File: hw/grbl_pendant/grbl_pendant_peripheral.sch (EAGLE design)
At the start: 29 parts, among them CON1 MOLEX-53261-0671, IC2 FT232RL, Q1 14.7456 MHz, X1 PN61729-S

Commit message: sch/brd files updated
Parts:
- removed C1, C8, C9: 10u, rcl:C-EUC0805
- removed C10: 100n, rcl:C-EUC0805
- removed C2, C4: 20p, rcl:C-EUC0603K
- removed C3: 100n, rcl:C-EUC0603
- removed C5, C6, C7: 100n, rcl:C-EUC0603K
- removed CON1: MOLEX-53261-0671, SchlegelAr_Master:MOLEX-53261-0671
- removed FERRIT1, FERRIT2, FERRIT3: (no value), rcl:R-EU_M0805
- removed IC2: FT232RL, ftdichip:FT232RL
- removed JP1: (no value), pinhead-2:PINHD-2X08_2.54
- removed Q1: 14.7456 MHz, crystal:CRYSTALHC49UP
- removed R2, R3, R7: 220R, rcl:R-EU_R0603
- removed R4, R5, R6: 100R, rcl:R-EU_R0603
- removed U$2: ARDUINONANO, rocketfarm:ARDUINONANO
- removed X1: PN61729-S, con-berg:PN61729-S
- removed X2, X3: (no value), con-subd:F25HPS
- added C11: 100n, rcl:C-EUC0603K
- added ENC1: ENCODER, encoder:ENCODER
- added IC1: 74HC595D, 74xx-eu:74HC595D
- added LED1, LED2, LED3, LED4, LED5, LED6, LED7, LED8: (no value), led:LED5MM
- added R10, R11, R12, R13, R14, R15, R8, R9: 680R, rcl:R-EU_R0603
- added R16, R17, R18, R19, R20, R21, R22, R23, R24, R25: 10k, rcl:R-EU_R0603
- added S1, S2, S3, S4, S5, S6, S7: (no value), switch-omron:10-XX
- added X4: (no value), con-subd:F25HPS
- R1: value 220R -> 10k; device rcl:R-EU_R0603 -> SchlegelAr_Master:35WR5KLFTR
- U$1: value MEGA162MA*A* -> LCD-HD447804-HOLES20X4-4HOLES; device avr-7:MEGA162MA*A* -> HD44780LCD:LCD-HD447804-HOLES20X4-4HOLES
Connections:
- removed net !RESET: CON1.RESET
- removed net COOLING_ENABLE: U$2.A3, X2-17.F
- removed net CYCLE_START/RESUME: U$2.A2, X2-18.F
- removed net FEED/HOLD: U$2.A1, X2-19.F
- removed net LED_SHIFT_SCK: U$1.(WR)PD6
- removed net LIMIT_INT_X: C9.2, FERRIT3.2, R1.2, R4.1
- removed net LIMIT_INT_Y: C8.2, FERRIT2.2, R3.2, R5.1
- removed net LIMIT_INT_Z: C1.2, FERRIT1.2, R2.2, R6.1
- removed net LIMIT_X: FERRIT3.1, X2-25.F
- removed net LIMIT_X_DEBOUNCED: R4.2, U$2.D9
- removed net LIMIT_Y: FERRIT2.1, X2-24.F
- removed net LIMIT_Y_DEBOUNCED: R5.2, U$2.D10
- removed net LIMIT_Z: FERRIT1.1, X2-23.F
- removed net LIMIT_Z_DEBOUNCED: R6.2, U$2.D11
- removed net MISO: CON1.MISO, JP1.13, JP1.14, U$1.(MISO)PB6
- removed net MOSI: CON1.MOSI, JP1.10, JP1.9, U$1.(MOSI)PB5
- removed net N$7: C4.2, Q1.2, U$1.XTAL2
- removed net N$8: C2.1, Q1.1, U$1.XTAL1
- removed net RESET/ABORT: U$2.A0, X2-20.F
- removed net RESET_AVR: U$1.RESET, U$2.RESET1, X2-21.F
- removed net RXD_BRIDGE: U$1.(RXD1)PB2, U$2.D1/TX
- removed net RXD_PC: IC2.RXD, U$1.(TXD0)PD1
- removed net SCK: CON1.SCK, JP1.11, JP1.12, U$1.(SCK)PB7
- removed net SD_IO_1: U$1.(AD7)PA7
- removed net SD_IO_2: U$1.(T1)PB1
- removed net SD_IO_3: U$1.(T0)PB0
- removed net SD_IO_4: U$1.(RD)PD7
- removed net SPINDLE_DIR: U$2.D13, X2-16.F
- removed net SPINDLE_ENABLE: U$2.D12, X2-1.F
- removed net SS: JP1.7, JP1.8, U$1.(SS)PB4
- removed net STEPPER_DISABLE: U$2.D8, X2-15.F
- removed net TXD_BRIDGE: U$1.(TXD1)PB3, U$2.D0/RX
- removed net TXD_PC: IC2.TXD, U$1.(RXD0)PD0
- removed net USBDM: IC2.USBDM, X1.2
- removed net USBDP: IC2.USBDP, X1.3
- removed net X_DIR: U$2.D5, X2-2.F
- removed net X_STEP: U$2.D2, X2-3.F
- removed net Y_DIR: U$2.D6, X2-4.F
- removed net Y_STEP: U$2.D3, X2-5.F
- removed net Z_DIR: U$2.D7, X2-6.F
- removed net Z_PROBE: R7.2, U$2.A5, X2-22.F
- removed net Z_STEP: U$2.D4, X2-7.F
- new net N$1: IC1A.QD, R11.1
- new net N$10: IC1A.QG, R14.1
- new net N$11: IC1A.QH, R15.1
- new net N$12: LED1.A, R8.2
- new net N$13: LED2.A, R9.2
- new net N$14: LED3.A, R10.2
- new net N$15: LED4.A, R11.2
- new net N$16: LED5.A, R12.2
- new net N$17: LED6.A, R13.2
- new net N$18: LED7.A, R14.2
- new net N$19: LED8.A, R15.2
- new net N$2: IC1A.QA, R8.1
- new net N$3: IC1A.QB, R9.1
- new net N$4: IC1A.QC, R10.1
- new net N$6: IC1A.QE, R12.1
- new net N$9: IC1A.QF, R13.1
- net +5V: now also C11.1, IC1A.SCL, IC1P.VCC, R1.E, R16.1, R17.1, R18.1, R19.1, R20.1, R21.1, R22.1, R23.1, R24.1, R25.1, U$1.A, U$1.VDD, X4-1.F; no longer C10.1, C5.1, C6.1, C7.1, CON1.VCC, IC2.!RESET, IC2.VCC, JP1.5, JP1.6, R1.1, R2.1, R3.1, R7.1, U$1.VCC, U$1.VCC1, U$1.VCC2, U$2.+5V, X1.1, X2-8.F, X2-9.F, X3-1.F
- net BTN1: now also R16.2, S1.P, S1.P1, X4-19.F; no longer U$1.(AD0)PA0, X3-19.F
- net BTN2: now also R17.2, S2.P, S2.P1, X4-18.F; no longer U$1.(AD1)PA1, X3-18.F
- net BTN3: now also R18.2, S3.P, S3.P1, X4-17.F; no longer U$1.(AD2)PA2, X3-17.F
- net BTN4: now also R19.2, S4.P, S4.P1, X4-16.F; no longer U$1.(AD3)PA3, X3-16.F
- net BTN5: now also R20.2, S5.P, S5.P1, X4-15.F; no longer U$1.(AD4)PA4, X3-15.F
- net BTN6: now also R21.2, S6.P, S6.P1, X4-14.F; no longer U$1.(AD5)PA5, X3-14.F
- net BTN_JOG: now also R25.2, S7.P, S7.P1, X4-13.F; no longer U$1.(AD6)PA6, X3-13.F
- net DISP_D0: now also U$1.DB0, X4-3.F; no longer U$1.(A8)PC0, X3-3.F
- net DISP_D1: now also U$1.DB1, X4-4.F; no longer U$1.(A9)PC1, X3-4.F
- net DISP_D2: now also U$1.DB2, X4-5.F; no longer U$1.(A10)PC2, X3-5.F
- net DISP_D3: now also U$1.DB3, X4-6.F; no longer U$1.(A11)PC3, X3-6.F
- net DISP_D4: now also U$1.DB4, X4-7.F; no longer U$1.(A12)PC4, X3-7.F
- net DISP_D5: now also U$1.DB5, X4-8.F; no longer U$1.(A13)PC5, X3-8.F
- net DISP_D6: now also U$1.DB6, X4-9.F; no longer U$1.(A14)PC6, X3-9.F
- net DISP_D7: now also U$1.DB7, X4-10.F; no longer U$1.(A15)PC7, X3-10.F
- net DISP_ENABLE: now also U$1.E, X4-12.F; no longer U$1.(ALE)PE1, X3-12.F
- net DISP_RS: now also U$1.RS, X4-11.F; no longer U$1.(OC1B)PE2, X3-11.F
- net ENCODER_A: now also ENC1.A, R23.2, X4-20.F; no longer U$1.(INT0)PD2, X3-20.F
- net ENCODER_B: now also ENC1.C, R24.2, X4-21.F; no longer U$1.(INT1)PD3, X3-21.F
- net ENCODER_BTN: now also ENC1.D, R22.2, X4-22.F; no longer U$1.(INT2)PE0, X3-22.F
- net GND: now also C11.2, ENC1.B, ENC1.E, IC1P.GND, LED1.C, LED2.C, LED3.C, LED4.C, LED5.C, LED6.C, LED7.C, LED8.C, R1.A, S1.S, S1.S1, S2.S, S2.S1, S3.S, S3.S1, S4.S, S4.S1, S5.S, S5.S1, S6.S, S6.S1, S7.S, S7.S1, U$1.K, U$1.R/W, U$1.VSS, X4-2.F; no longer C1.1, C10.2, C2.2, C3.1, C4.1, C5.2, C6.2, C7.2, C8.1, C9.1, CON1.GND, CON1.GND@1, CON1.GND@2, IC2.GND, IC2.GND@1, IC2.GND@2, IC2.TEST, JP1.1, JP1.15, JP1.16, JP1.2, U$1.GND, U$1.GND1, U$1.GND2, U$2.GND, U$2.GND1, X1.4, X1.S1, X1.S2, X2-10.F, X2-11.F, X2-12.F, X2-13.F, X3-2.F
- net LED_SHIFT_RCK: now also X4-23.F, X4-24.F; no longer U$1.(TOSC2)PD5, X3-23.F, X3-24.F
- net LED_SHIFT_SI: now also X4-25.F; no longer U$1.(TOSC1)PD4, X3-25.F
- net N$5: now also R1.S, U$1.VO; no longer C3.2, IC2.3V3OUT, IC2.VCCIO

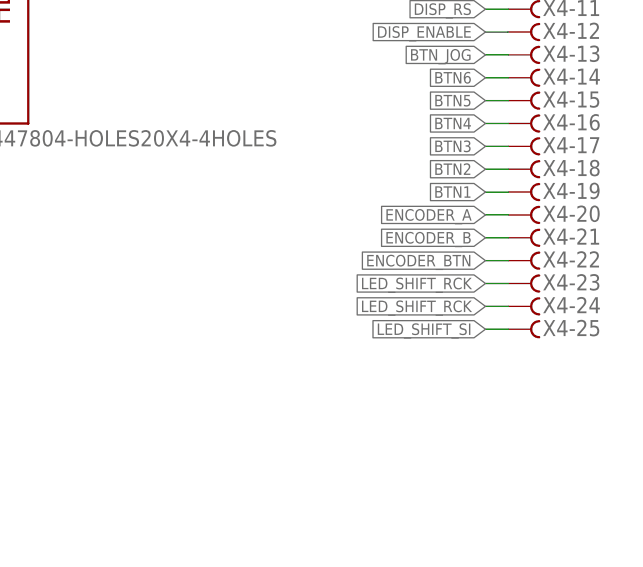
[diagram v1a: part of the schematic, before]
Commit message: grbl_pendant_peripheral v1 layout
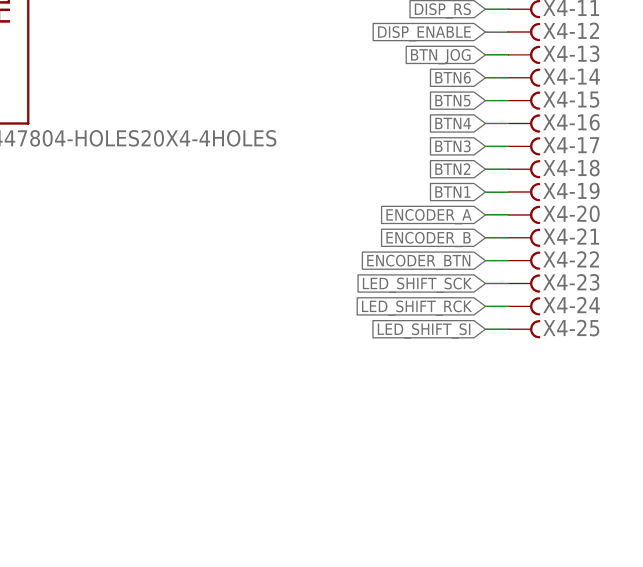
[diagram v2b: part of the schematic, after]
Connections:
- new net LED_SHIFT_SCK: IC1A.SCK, X4-23.F
- net LED_SHIFT_RCK: now also IC1A.RCK; no longer X4-23.F
- net LED_SHIFT_SI: now also IC1A.SER
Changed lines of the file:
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@@
 <wire x1="45.72" y1="147.32" x2="43.18" y2="147.32" width="0.1524" layer="91"/>
 <label x="43.18" y="147.32" size="1.27" layer="95" rot="R180" xref="yes"/>
+<pinref part="IC1" gate="A" pin="SER"/>
 </segment>
 <segment>
@@
 <net name="LED_SHIFT_RCK" class="0">
 <segment>
+<label x="43.18" y="134.62" size="1.27" layer="95" rot="R180" xref="yes"/>
 <wire x1="45.72" y1="134.62" x2="43.18" y2="134.62" width="0.1524" layer="91"/>
-<label x="43.18" y="134.62" size="1.27" layer="95" rot="R180" xref="yes"/>
+<pinref part="IC1" gate="A" pin="RCK"/>
 </segment>
 <segment>
-<pinref part="X4" gate="-23" pin="F"/>
-<wire x1="236.22" y1="60.96" x2="233.68" y2="60.96" width="0.1524" layer="91"/>
-<label x="233.68" y="60.96" size="1.27" layer="95" rot="R180" xref="yes"/>
-</segment>
-<segment>
+<label x="233.68" y="58.42" size="1.27" layer="95" rot="R180" xref="yes"/>
+<wire x1="236.22" y1="58.42" x2="233.68" y2="58.42" width="0.1524" layer="91"/>
 <pinref part="X4" gate="-24" pin="F"/>
-<wire x1="236.22" y1="58.42" x2="233.68" y2="58.42" width="0.1524" layer="91"/>
-<label x="233.68" y="58.42" size="1.27" layer="95" rot="R180" xref="yes"/>
 </segment>
 </net>
 <net name="LED_SHIFT_SCK" class="0">
 <segment>
+<label x="43.18" y="142.24" size="1.27" layer="95" rot="R180" xref="yes"/>
 <wire x1="45.72" y1="142.24" x2="43.18" y2="142.24" width="0.1524" layer="91"/>
-<label x="43.18" y="142.24" size="1.27" layer="95" rot="R180" xref="yes"/>
+<pinref part="IC1" gate="A" pin="SCK"/>
+</segment>
+<segment>
+<label x="233.68" y="60.96" size="1.27" layer="95" rot="R180" xref="yes"/>
+<wire x1="236.22" y1="60.96" x2="233.68" y2="60.96" width="0.1524" layer="91"/>
+<pinref part="X4" gate="-23" pin="F"/>
 </segment>
 </net>
